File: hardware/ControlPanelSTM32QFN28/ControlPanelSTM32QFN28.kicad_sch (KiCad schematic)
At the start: 19 parts, among them J1 8P8C, J10 Conn_01x04_Male, J11 Conn_01x04_Male, J12 Conn_01x02_Male, J13 Conn_01x02_Male, J14 Conn_01x02_Male, J15 Conn_01x02_Male, J4 Conn_02x03, J5 Conn_01x04_Male, J6 Conn_01x04_Male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

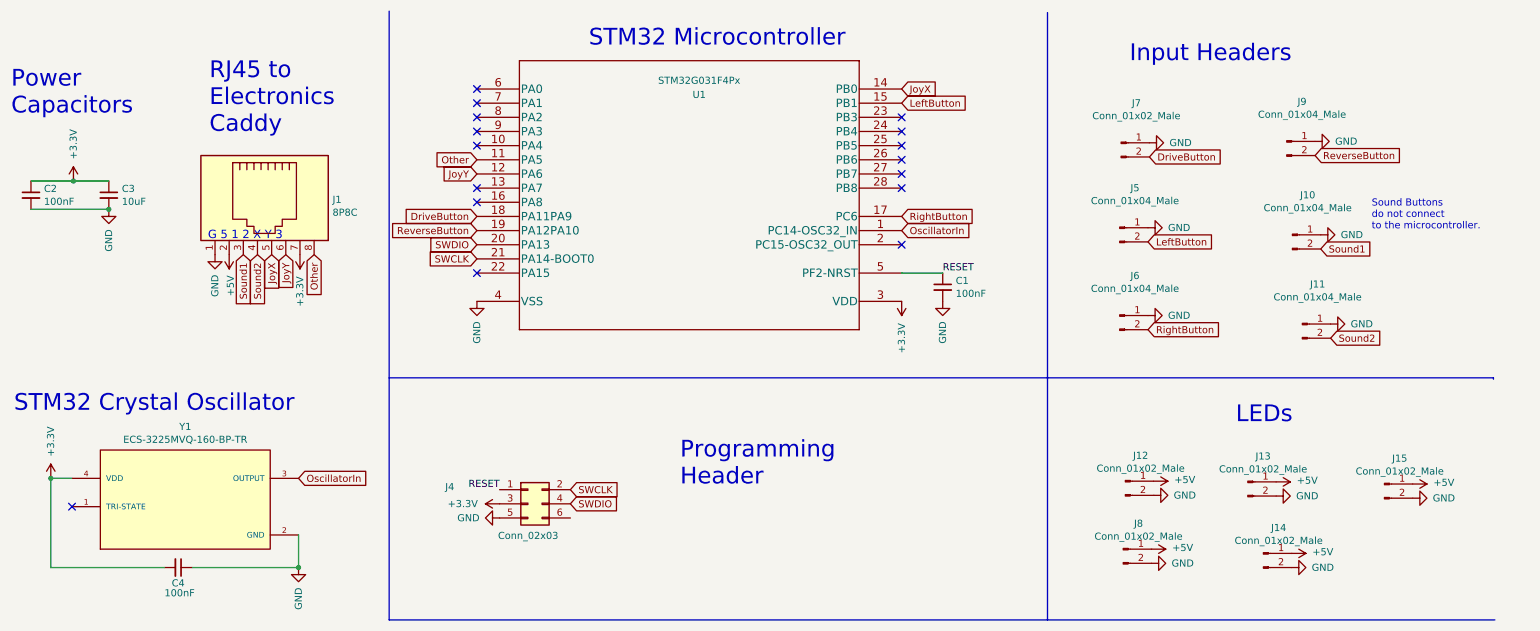
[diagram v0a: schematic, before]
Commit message: updating control panel PCB to use new programming header, smaller SMDs and with JLCPCB part numbers
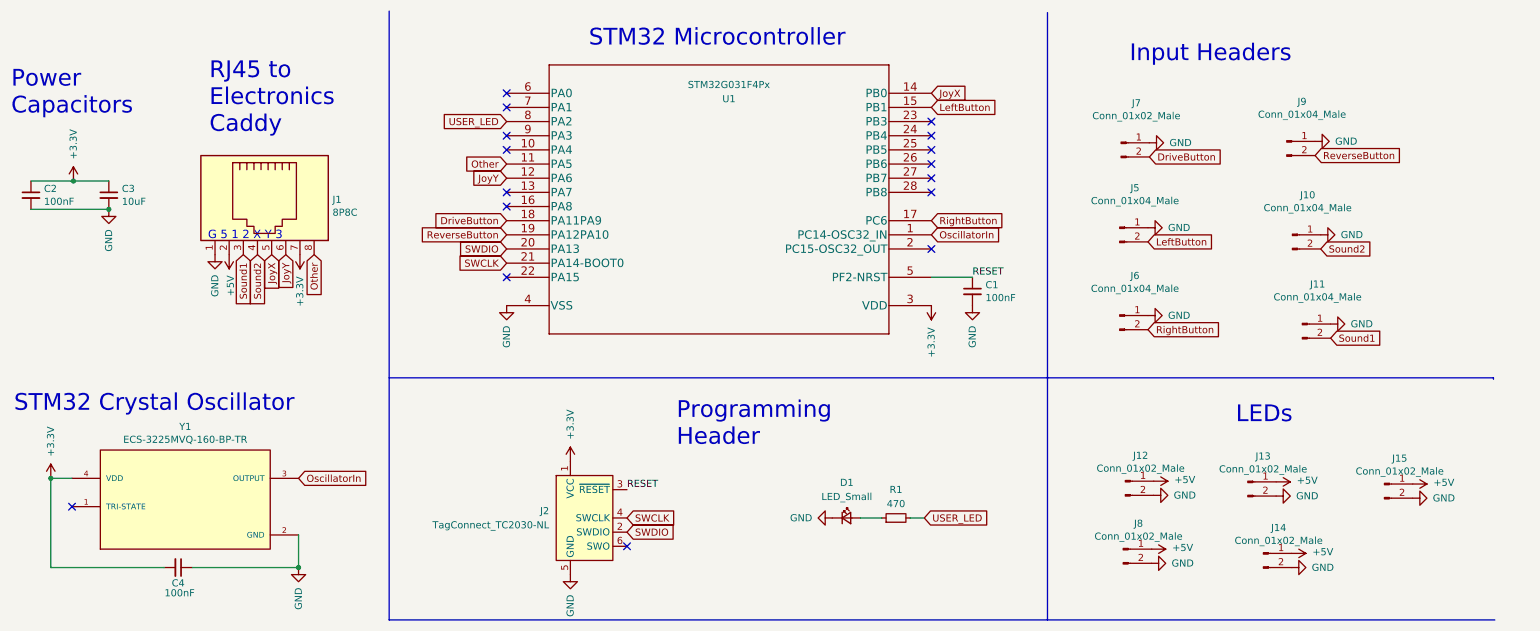
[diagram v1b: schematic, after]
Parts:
- removed J4: Conn_02x03, Connector_PinHeader_2.54mm:PinHeader_2x03_P2.54mm_Vertical, symbol Connector_Generic:Conn_02x03_Odd_Even
- added D1: LED_Small, Capacitor_SMD:C_0603_1608Metric, symbol Device:LED_Small
- added J2: TagConnect_TC2030-NL, Connector:Tag-Connect_TC2030-IDC-NL_2x03_P1.27mm_Vertical, symbol Connector:Conn_ARM_SWD_TagConnect_TC2030-NL
- added R1: 470, Capacitor_SMD:C_0402_1005Metric, symbol Device:R_Small
- C1, C2, C4: footprint Capacitor_SMD:C_0805_2012Metric -> Capacitor_SMD:C_0402_1005Metric; MPN (none) -> C307331
- C3: footprint Capacitor_SMD:C_0805_2012Metric -> Capacitor_SMD:C_0603_1608Metric; MPN (none) -> C96446
- J10, J11, J12, J13, J14, J15, J5, J6, J7, J8, J9: MPN (none) -> C158012
- U1: MPN (none) -> C432211
- Y1: MPN (none) -> C252336
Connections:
- net +3V3: now also J2.1 (VCC)
- net GND: now also D1.1 (K), J2.5 (GND)
- net RESET: now also J2.3 (~{RESET})
- net SWCLK: now also J2.4 (SWCLK)
- net SWDIO: now also J2.2 (SWDIO)
- net Sound1: now also J11.2 (Pin_2); no longer J10.2 (Pin_2)
- net Sound2: now also J10.2 (Pin_2); no longer J11.2 (Pin_2)
- net USER_LED: now reaches U1.8 (PA2)
- net USER_LED: now also R1.2
- new net: D1.2 (A), R1.1
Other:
- note removed: "Sound Buttons do not connect to the microcontroller."
- moved on the sheet: C1, U1
